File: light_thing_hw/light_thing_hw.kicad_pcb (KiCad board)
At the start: 2 copper layers, 50 x 50 mm, 58 parts, among them J1 CONNECTORS, J2 Li-Ion Battery, J3 ADDR_LED_PANEL_1_CONNECTORS, J4 ADDR_LED_PANEL_2_CONNECTORS, J5 MIC_CONN, Q1 MMBF170, SW1 ST_USER_BUTTON1, SW2 ST_RESET_BUTTON, U1 BC832-V1, U2 LSM6DS3, U3 MCP73833T-FCI_UN, U4 LMR62421XMF, U5 LP38511MRX-ADJ_NOPB, U5A1 STM32L452RETx

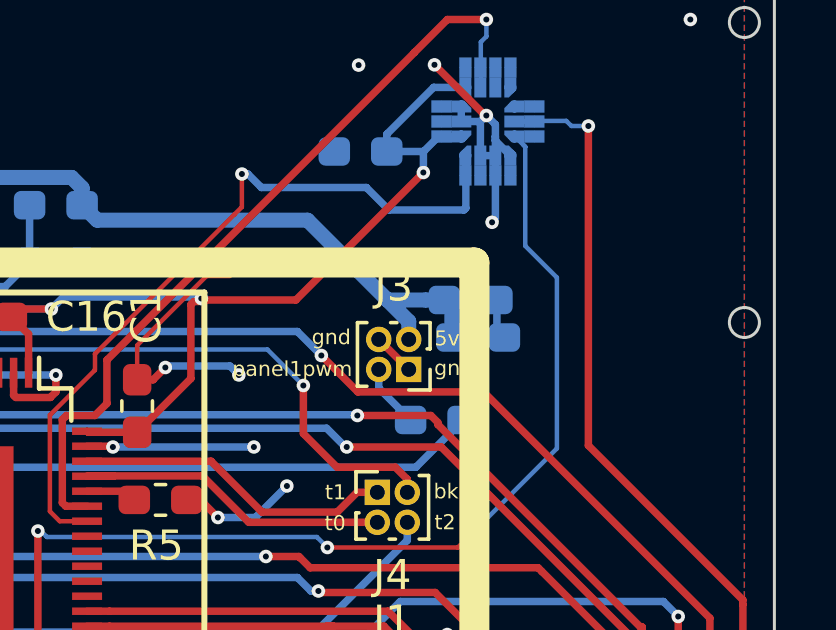
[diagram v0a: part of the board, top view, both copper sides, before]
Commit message: some sw changes. about to add another mosfet switch to the board for the mic
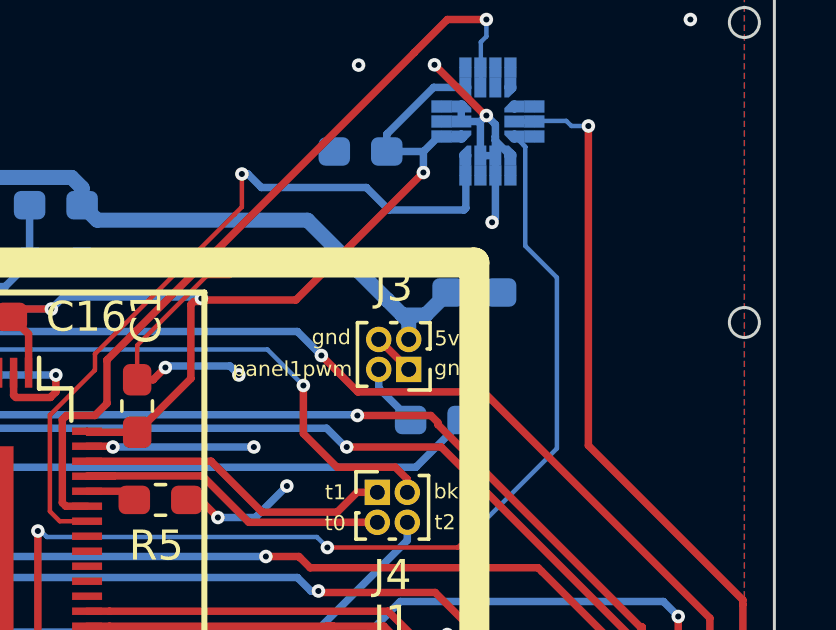
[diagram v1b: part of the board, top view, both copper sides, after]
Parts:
- removed 1000uF1: C_Small, Capacitor_SMD:C_0603_1608Metric_Pad1.05x0.95mm_HandSolder
- C7: value C_Small -> 1000uF
- moved C7 0.28 mm to (159.5, 76.2)
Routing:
- net +5V: track 26.2 -> 24.8 mm
- net GND: track 137.4 -> 136.2 mm
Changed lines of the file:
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@@
     (thickness 1.6)
     (drawings 114)
-    (tracks 897)
+    (tracks 895)
     (zones 0)
-    (modules 58)
+    (modules 57)
     (nets 102)
   )
@@
     (add_net VBUS)
   )
+  (module Capacitor_SMD:C_0603_1608Metric_Pad1.05x0.95mm_HandSolder (layer B.Cu)
+    (at 159.5 76.25)
+    (descr "Capacitor SMD 0603 (1608 Metric), square (rectangular) end terminal, IPC_7351 nominal with elongated pad for handsoldering. (Body size source: http://www.tortai-tech.com/upload/download/2011102023233369053.pdf), generated with kicad-footprint-generator")
+    (tags "capacitor handsolder")
+    (attr smd)
+    (fp_text reference C7 (at 2.5 0) (layer B.SilkS)
+      (effects (font (size 1 1) (thickness 0.15)) (justify mirror))
+    )
+    (fp_text value 1000uF (at 0 -1.43) (layer B.Fab)
+      (effects (font (size 1 1) (thickness 0.15)) (justify mirror))
+    )
+    (fp_line (start -0.8 -0.4) (end -0.8 0.4) (layer B.Fab) (width 0.1))
+    (fp_line (start -0.8 0.4) (end 0.8 0.4) (layer B.Fab) (width 0.1))
+    (fp_line (start 0.8 0.4) (end 0.8 -0.4) (layer B.Fab) (width 0.1))
+    (fp_line (start 0.8 -0.4) (end -0.8 -0.4) (layer B.Fab) (width 0.1))
+    (fp_line (start -0.171267 0.51) (end 0.171267 0.51) (layer B.SilkS) (width 0.12))
+    (fp_line (start -0.171267 -0.51) (end 0.171267 -0.51) (layer B.SilkS) (width 0.12))
+    (fp_line (start -1.65 -0.73) (end -1.65 0.73) (layer B.CrtYd) (width 0.05))
+    (fp_line (start -1.65 0.73) (end 1.65 0.73) (layer B.CrtYd) (width 0.05))
+    (fp_line (start 1.65 0.73) (end 1.65 -0.73) (layer B.CrtYd) (width 0.05))
+    (fp_line (start 1.65 -0.73) (end -1.65 -0.73) (layer B.CrtYd) (width 0.05))
+    (fp_text user %R (at 0 0) (layer B.Fab)
+      (effects (font (size 0.4 0.4) (thickness 0.06)) (justify mirror))
+    )
+    (pad 1 smd roundrect (at -0.875 0) (size 1.05 0.95) (layers B.Cu B.Paste B.Mask) (roundrect_rratio 0.25)
+      (net 4 +5V))
+    (pad 2 smd roundrect (at 0.875 0) (size 1.05 0.95) (layers B.Cu B.Paste B.Mask) (roundrect_rratio 0.25)
+      (net 90 GND))
+    (model ${KISYS3DMOD}/Capacitor_SMD.3dshapes/C_0603_1608Metric.wrl
+      (at (xyz 0 0 0))
+      (scale (xyz 1 1 1))
+      (rotate (xyz 0 0 0))
+    )
+  )
   (module Connector_PinHeader_1.00mm:PinHeader_1x03_P1.00mm_Vertical (layer F.Cu)
     (at 131.5 80.25)
@@
   )
   (module Capacitor_SMD:C_0603_1608Metric_Pad1.05x0.95mm_HandSolder (layer B.Cu)
-    (at 159.375 76.5)
-    (descr "Capacitor SMD 0603 (1608 Metric), square (rectangular) end terminal, IPC_7351 nominal with elongated pad for handsoldering. (Body size source: http://www.tortai-tech.com/upload/download/2011102023233369053.pdf), generated with kicad-footprint-generator")
-    (tags "capacitor handsolder")
-    (attr smd)
-    (fp_text reference C7 (at 0.875 1.5) (layer B.SilkS)
-      (effects (font (size 1 1) (thickness 0.15)) (justify mirror))
-    )
-    (fp_text value C_Small (at 0 -1.43) (layer B.Fab)
-      (effects (font (size 1 1) (thickness 0.15)) (justify mirror))
-    )
-    (fp_line (start -0.8 -0.4) (end -0.8 0.4) (layer B.Fab) (width 0.1))
-    (fp_line (start -0.8 0.4) (end 0.8 0.4) (layer B.Fab) (width 0.1))
-    (fp_line (start 0.8 0.4) (end 0.8 -0.4) (layer B.Fab) (width 0.1))
-    (fp_line (start 0.8 -0.4) (end -0.8 -0.4) (layer B.Fab) (width 0.1))
-    (fp_line (start -0.171267 0.51) (end 0.171267 0.51) (layer B.SilkS) (width 0.12))
-    (fp_line (start -0.171267 -0.51) (end 0.171267 -0.51) (layer B.SilkS) (width 0.12))
-    (fp_line (start -1.65 -0.73) (end -1.65 0.73) (layer B.CrtYd) (width 0.05))
-    (fp_line (start -1.65 0.73) (end 1.65 0.73) (layer B.CrtYd) (width 0.05))
-    (fp_line (start 1.65 0.73) (end 1.65 -0.73) (layer B.CrtYd) (width 0.05))
-    (fp_line (start 1.65 -0.73) (end -1.65 -0.73) (layer B.CrtYd) (width 0.05))
-    (fp_text user %R (at 0 0) (layer B.Fab)
-      (effects (font (size 0.4 0.4) (thickness 0.06)) (justify mirror))
-    )
-    (pad 1 smd roundrect (at -0.875 0) (size 1.05 0.95) (layers B.Cu B.Paste B.Mask) (roundrect_rratio 0.25)
-      (net 4 +5V))
-    (pad 2 smd roundrect (at 0.875 0) (size 1.05 0.95) (layers B.Cu B.Paste B.Mask) (roundrect_rratio 0.25)
-      (net 90 GND))
-    (model ${KISYS3DMOD}/Capacitor_SMD.3dshapes/C_0603_1608Metric.wrl
-      (at (xyz 0 0 0))
-      (scale (xyz 1 1 1))
-      (rotate (xyz 0 0 0))
-    )
-  )
-  (module Capacitor_SMD:C_0603_1608Metric_Pad1.05x0.95mm_HandSolder (layer B.Cu)
     (at 134.245 73.11)
     (descr "Capacitor SMD 0603 (1608 Metric), square (rectangular) end terminal, IPC_7351 nominal with elongated pad for handsoldering. (Body size source: http://www.tortai-tech.com/upload/download/2011102023233369053.pdf), generated with kicad-footprint-generator")
@@
     )
   )
-  (module Capacitor_SMD:C_0603_1608Metric_Pad1.05x0.95mm_HandSolder (layer B.Cu)
-    (at 159.625 77.75)
-    (descr "Capacitor SMD 0603 (1608 Metric), square (rectangular) end terminal, IPC_7351 nominal with elongated pad for handsoldering. (Body size source: http://www.tortai-tech.com/upload/download/2011102023233369053.pdf), generated with kicad-footprint-generator")
-    (tags "capacitor handsolder")
-    (attr smd)
-    (fp_text reference 1000uF1 (at 0 1.43) (layer B.SilkS)
-      (effects (font (size 1 1) (thickness 0.15)) (justify mirror))
-    )
-    (fp_text value C_Small (at 0 -1.43) (layer B.Fab)
-      (effects (font (size 1 1) (thickness 0.15)) (justify mirror))
-    )
-    (fp_line (start -0.8 -0.4) (end -0.8 0.4) (layer B.Fab) (width 0.1))
-    (fp_line (start -0.8 0.4) (end 0.8 0.4) (layer B.Fab) (width 0.1))
-    (fp_line (start 0.8 0.4) (end 0.8 -0.4) (layer B.Fab) (width 0.1))
-    (fp_line (start 0.8 -0.4) (end -0.8 -0.4) (layer B.Fab) (width 0.1))
-    (fp_line (start -0.171267 0.51) (end 0.171267 0.51) (layer B.SilkS) (width 0.12))
-    (fp_line (start -0.171267 -0.51) (end 0.171267 -0.51) (layer B.SilkS) (width 0.12))
-    (fp_line (start -1.65 -0.73) (end -1.65 0.73) (layer B.CrtYd) (width 0.05))
-    (fp_line (start -1.65 0.73) (end 1.65 0.73) (layer B.CrtYd) (width 0.05))
-    (fp_line (start 1.65 0.73) (end 1.65 -0.73) (layer B.CrtYd) (width 0.05))
-    (fp_line (start 1.65 -0.73) (end -1.65 -0.73) (layer B.CrtYd) (width 0.05))
-    (fp_text user %R (at 0 0) (layer B.Fab)
-      (effects (font (size 0.4 0.4) (thickness 0.06)) (justify mirror))
-    )
-    (pad 1 smd roundrect (at -0.875 0) (size 1.05 0.95) (layers B.Cu B.Paste B.Mask) (roundrect_rratio 0.25)
-      (net 4 +5V))
-    (pad 2 smd roundrect (at 0.875 0) (size 1.05 0.95) (layers B.Cu B.Paste B.Mask) (roundrect_rratio 0.25)
-      (net 90 GND))
-    (model ${KISYS3DMOD}/Capacitor_SMD.3dshapes/C_0603_1608Metric.wrl
-      (at (xyz 0 0 0))
-      (scale (xyz 1 1 1))
-      (rotate (xyz 0 0 0))
-    )
-  )
   (gr_line (start 128.25 79.25) (end 132.5 79.25) (layer B.SilkS) (width 0.2))
   (gr_line (start 128.25 83.25) (end 128.25 79.25) (layer B.SilkS) (width 0.2))
@@
   (segment (start 143.5 72.41499) (end 142.96501 72.41499) (width 0.5) (layer B.Cu) (net 4))
   (segment (start 146.07499 72.41499) (end 143.5 72.41499) (width 0.5) (layer B.Cu) (net 4))
-  (segment (start 158.5 76.5) (end 157.875 76.5) (width 0.5) (layer B.Cu) (net 4))
-  (segment (start 157.875 76.5) (end 156.599648 76.5) (width 0.5) (layer B.Cu) (net 4))
   (segment (start 153.93872 73.839072) (end 156.599648 76.5) (width 0.5) (layer B.Cu) (net 4))
-  (segment (start 156.599648 76.5) (end 157.31274 77.213092) (width 0.5) (layer B.Cu) (net 4))
-  (segment (start 158.75 76.75) (end 158.5 76.5) (width 0.5) (layer B.Cu) (net 4))
-  (segment (start 158.75 77.75) (end 158.75 76.75) (width 0.5) (layer B.Cu) (net 4))
+  (segment (start 157.875 77) (end 158.625 76.25) (width 0.5) (layer B.Cu) (net 4))
+  (segment (start 157.099648 77) (end 157.875 77) (width 0.5) (layer B.Cu) (net 4))
+  (segment (start 157.099648 77) (end 157.31274 77.213092) (width 0.5) (layer B.Cu) (net 4))
+  (segment (start 156.599648 76.5) (end 157.099648 77) (width 0.5) (layer B.Cu) (net 4))
   (segment (start 137.968804 101.933155) (end 137.968804 101.450555) (width 0.25) (layer B.Cu) (net 5) (status 30))
   (segment (start 139.403404 101.933155) (end 139.911404 102.441155) (width 0.25) (layer B.Cu) (net 5) (status 20))
@@
   (segment (start 159.9 70.35) (end 159.86 70.35) (width 0.25) (layer F.Cu) (net 90))
   (via (at 155.64 68.67) (size 0.45) (drill 0.2) (layers F.Cu B.Cu) (net 90))
-  (segment (start 160.25 77.75) (end 160.25 76.5) (width 0.25) (layer B.Cu) (net 90))
   (segment (start 132.513695 83.263695) (end 131.5 82.25) (width 0.25) (layer F.Cu) (net 90))
   (segment (start 133.399571 83.263695) (end 132.513695 83.263695) (width 0.25) (layer F.Cu) (net 90))

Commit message: about to change user button
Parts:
- added Q2: BSS83P, Package_TO_SOT_SMD:SOT-23, B.Cu at (129.9, 74.2)
- SW2: footprint Button_Switch_SMD:SW_SPST_CK_RS282G05A3 -> Button_Switch_SMD:SW_SPST_EVPBF
- moved R9 3.36 mm to (126.1, 69.8)
- moved SW2 3.17 mm to (137.3, 99.0)
- moved R8 2.31 mm to (126.1, 68.2)
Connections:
- J5 pad 2: +3V3 -> MIC_3V3
- U5A1 pad 28: Net-(U5A1-Pad28) -> MIC_ENABLE
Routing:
- net MIC_ENABLE: track 0.00 -> 14.6 mm, vias 0 -> 1
- net MIC_3V3: track 0.00 -> 12.5 mm
- net CHARGER_STAT2: track 23.5 -> 35.0 mm
- net CHARGER_STAT1: track 14.0 -> 21.3 mm
- net RESET: track 88.0 -> 93.8 mm
- net GND: track 136.2 -> 140.3 mm, vias 31 -> 33
- net BATT_ADC: track 51.7 -> 55.3 mm
- net BT_RED_LED: track 65.4 -> 68.0 mm
- net GREEN_LED: track 18.8 -> 21.3 mm
- net +3V3: track 166.1 -> 168.2 mm, vias 13 -> 14
- net Net-(D3-Pad2): track 3.10 -> 4.35 mm
- net USART_2_RX: track 52.4 -> 51.5 mm

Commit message: hw updates. sent to print
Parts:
- added C19: 220uF, Capacitor_SMD:C_0603_1608Metric_Pad1.05x0.95mm_HandSolder, B.Cu at (160.3, 78.3)
- added C20: 220uF, Capacitor_SMD:C_0603_1608Metric_Pad1.05x0.95mm_HandSolder, B.Cu at (160.3, 77.0)
- C7: value 1000uF -> 220uF
- moved C7 0.66 mm to (159.4, 75.6)
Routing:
- net +5V: track 24.8 -> 28.3 mm

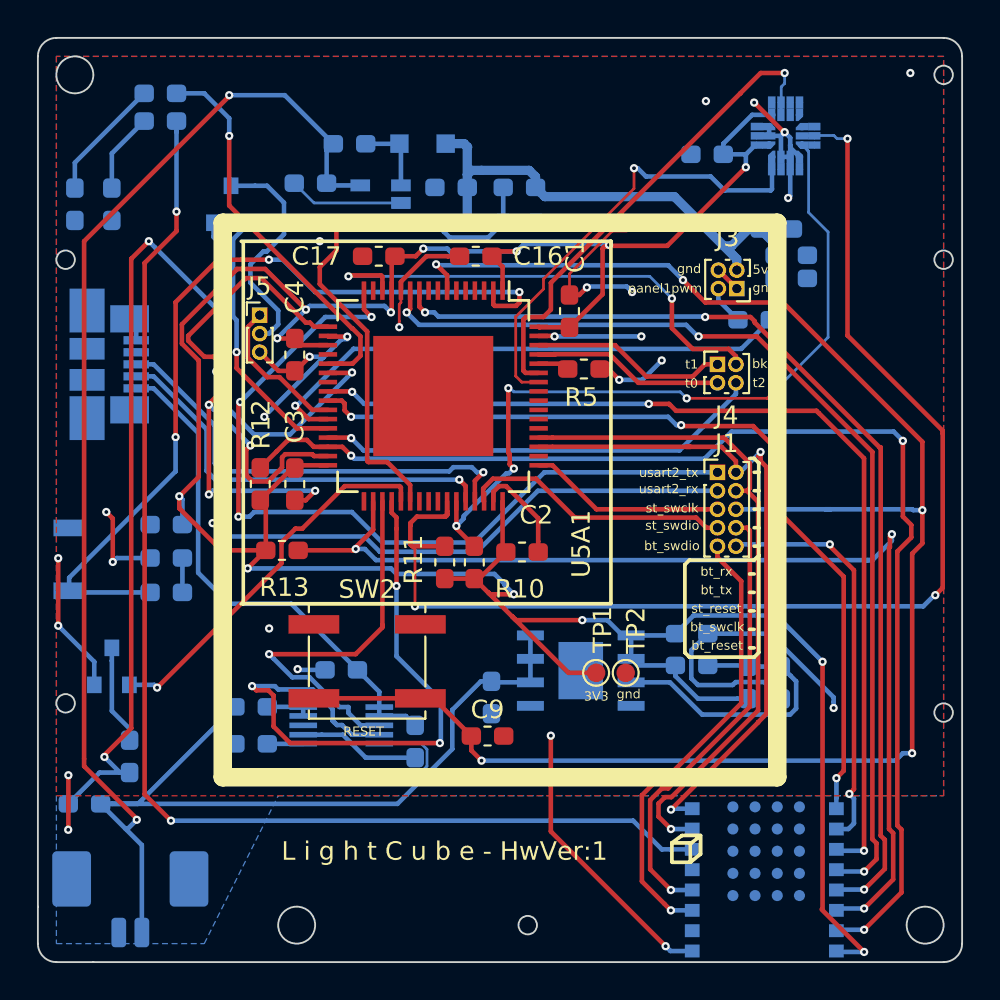
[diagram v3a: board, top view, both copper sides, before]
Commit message: moved to STM32L476
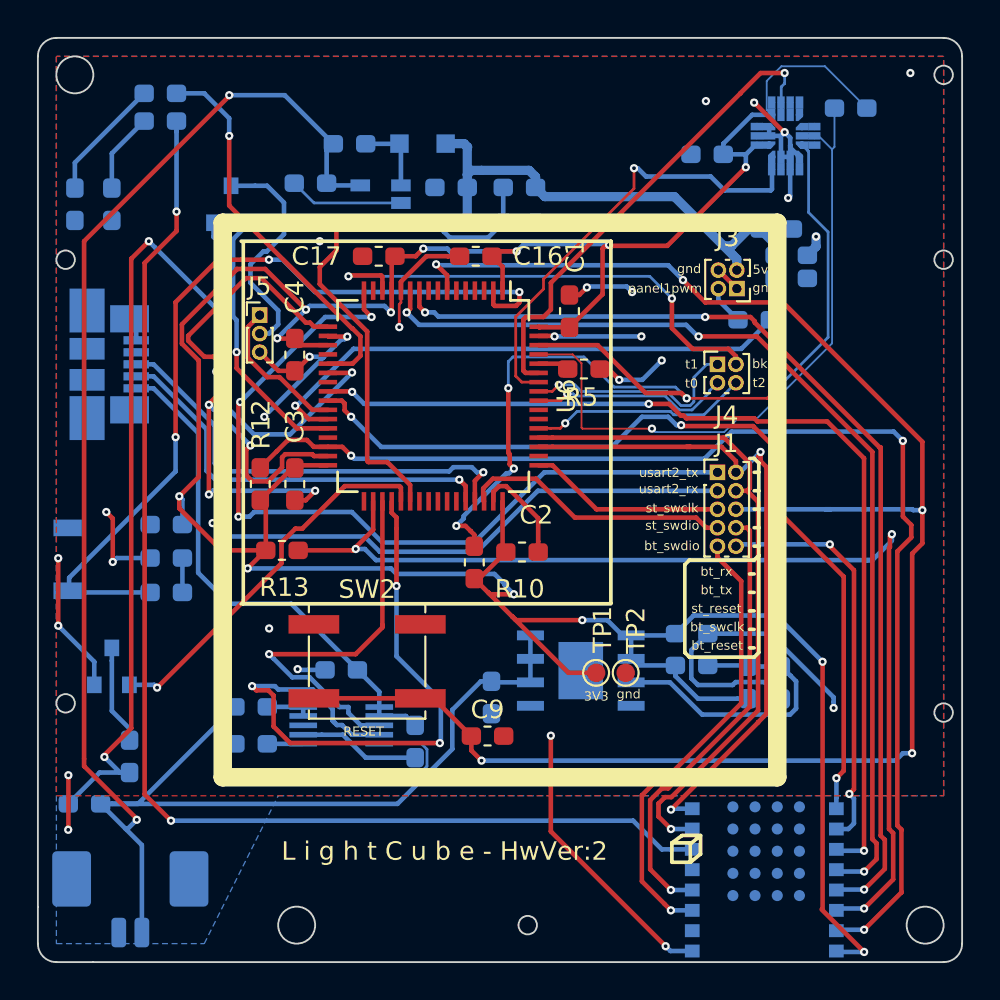
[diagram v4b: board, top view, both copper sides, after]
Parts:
- removed U5A1: STM32L452RETx, Package_QFP:LQFP-64-1EP_10x10mm_P0.5mm_EP6.5x6.5mm
- added U6: STM32L476RGTx, Package_QFP:LQFP-64_10x10mm_P0.5mm, F.Cu at (140.9, 84.6)
- R11: moved to B.Cu
- moved R11 33.0 mm to (163.5, 69.0), turned to 180 degrees
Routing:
- net I2C1_SCL: track 67.6 -> 37.3 mm, vias 3 -> 1
- net TEST_GPIO2: track 24.2 -> 11.8 mm
- net I2C1_SDA: track 41.6 -> 52.0 mm
- net +3V3: track 168.2 -> 175.2 mm
- net GND: track 140.3 -> 136.4 mm, vias 33 -> 34
- net BT_GPIO_3: track 46.4 -> 48.0 mm
- net TEST_GPIO1: track 10.7 -> 12.0 mm, vias 0 -> 1
- net TEST_GPIO0: track 11.2 -> 10.8 mm, vias 0 -> 1
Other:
- board text added: "L i g h t C u b e - HwVer:2"
- board text removed: "L i g h t C u b e - HwVer:1"

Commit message: about to change diode footprint to something thats available in digikey
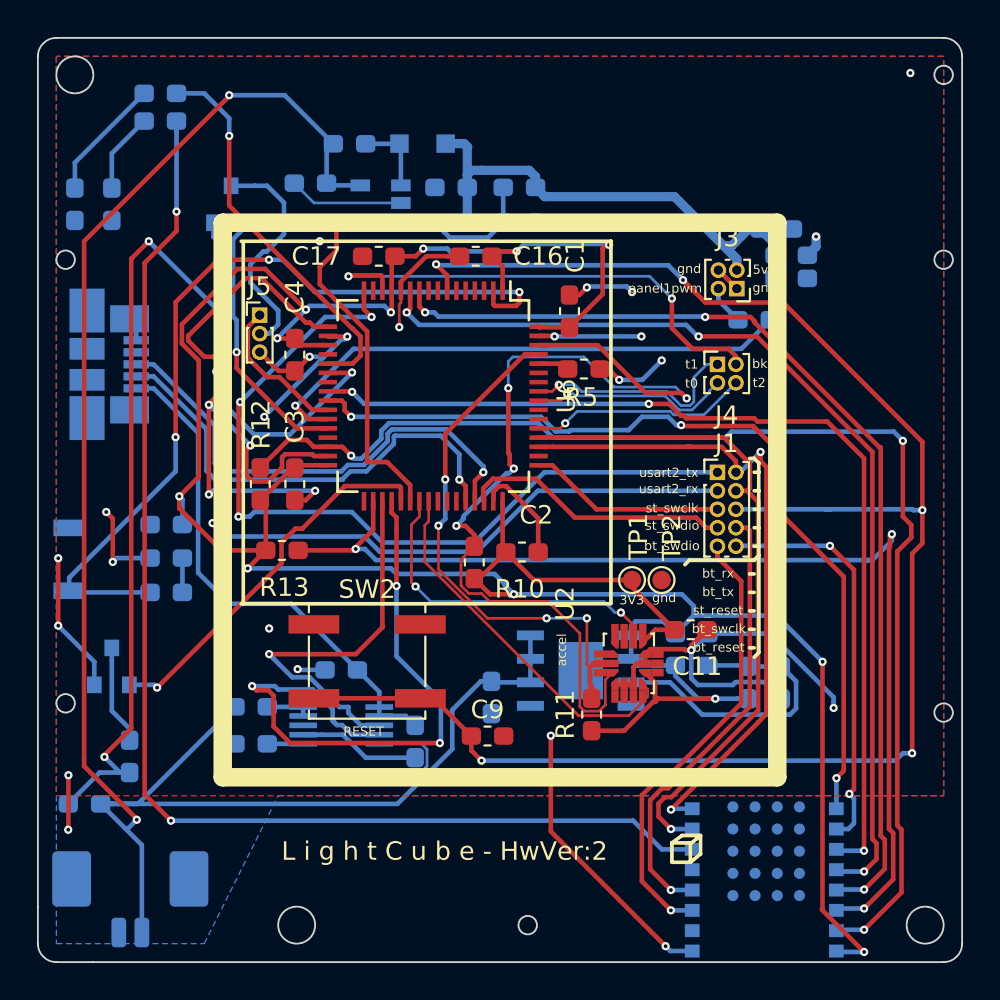
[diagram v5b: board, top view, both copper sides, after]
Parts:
- C11, R11, U2: moved to F.Cu
- moved R11 35.7 mm to (149.5, 101.9), turned to 90 degrees
- moved U2 29.8 mm to (151.5, 99.1)
- moved C11 25.7 mm to (154.8, 97.3), turned to 0 degrees
- moved TP1 5.38 mm to (151.6, 94.6)
- moved TP2 5.38 mm to (153.2, 94.6)
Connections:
- U6 pad 39: Net-(U6-Pad39) -> ACCEL_EXTI_2
- U6 pad 40: Net-(U6-Pad40) -> ACCEL_EXTI_1
- U6 pad 58: ACCEL_EXTI_1 -> Net-(U6-Pad58)
- U6 pad 59: ACCEL_EXTI_2 -> Net-(U6-Pad59)
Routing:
- net I2C1_SCL: track 37.3 -> 29.2 mm, vias 1 -> 4
- net ACCEL_EXTI_2: track 26.5 -> 18.5 mm, vias 1 -> 2
- net +3V3: track 175.2 -> 169.9 mm, vias 14 -> 13
- net ACCEL_EXTI_1: track 25.0 -> 20.1 mm, vias 1 -> 0
- net D-: track 22.4 -> 25.5 mm
- net I2C1_SDA: track 52.0 -> 49.4 mm, vias 5 -> 4
- net D+: track 24.4 -> 26.5 mm
- net GND: track 136.4 -> 134.5 mm, vias 34 -> 31
- net I2C2_SDA: track 66.0 -> 66.9 mm
- net BT_GPIO_3: track 48.0 -> 47.3 mm
